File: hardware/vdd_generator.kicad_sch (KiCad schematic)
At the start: 26 parts, among them Q1 BC547, Q2 BC327, Q3 BC327, Q4 BC327, U2 74LS06N

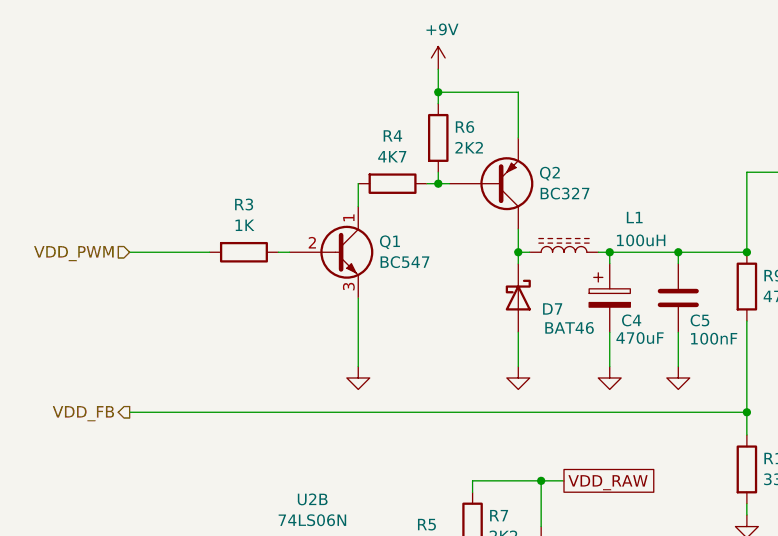
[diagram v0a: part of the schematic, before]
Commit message: Rev.E. Updated hardware design.
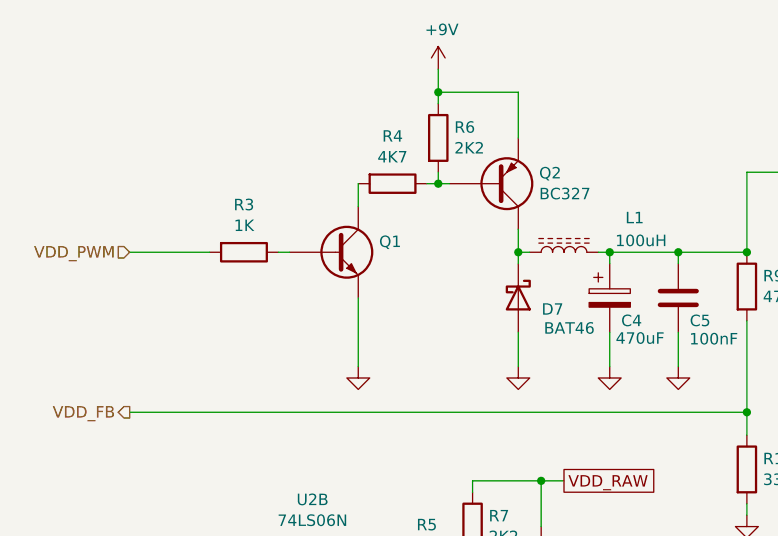
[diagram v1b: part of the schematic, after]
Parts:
- Q1: value BC547 -> (none); footprint Package_TO_SOT_THT:TO-92_Inline_Wide -> (none)
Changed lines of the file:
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@@
   (title_block
     (title "USB Flash/EPROM Programmer")
-    (date "2022-04-23")
+    (date "2022-04-27")
     (rev "v0.1.0 rev.E")
     (company "Robson Martins")
@@
       (effects (font (size 1.27 1.27)) (justify left))
     )
-    (property "Value" "BC547" (id 1) (at 62.0014 48.133 0)
-      (effects (font (size 1.27 1.27)) (justify left))
-    )
-    (property "Footprint" "Package_TO_SOT_THT:TO-92_Inline_Wide" (id 2) (at 62.23 48.895 0)
+    (property "Value" "" (id 1) (at 62.0014 48.133 0)
+      (effects (font (size 1.27 1.27)) (justify left))
+    )
+    (property "Footprint" "" (id 2) (at 62.23 48.895 0)
       (effects (font (size 1.27 1.27) italic) (justify left) hide)
     )

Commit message: Rev.E. Updated specifications document and hardware design.
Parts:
- C4: footprint Capacitor_THT:CP_Radial_D10.0mm_P7.50mm -> (none)
- C6: footprint Capacitor_THT:CP_Radial_D8.0mm_P3.50mm -> (none)
- Q2, Q3, Q4: value BC327 -> (none); footprint Package_TO_SOT_THT:TO-92_Inline_Wide -> (none)
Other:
- note added: "1/2W"
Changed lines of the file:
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@@
     (stroke (width 0) (type default) (color 0 0 0 0))
+  )
+  (text "1/2W" (at 138.43 77.47 0)
+    (effects (font (size 1.27 1.27)) (justify left bottom))
   )
   (text "5V1\n1W" (at 152.4 86.36 0)
@@
       (effects (font (size 1.27 1.27)) (justify left))
     )
-    (property "Footprint" "Capacitor_THT:CP_Radial_D10.0mm_P7.50mm" (id 2) (at 88.5952 55.88 0)
+    (property "Footprint" "" (id 2) (at 88.5952 55.88 0)
       (effects (font (size 1.27 1.27)) hide)
     )
@@
       (effects (font (size 1.27 1.27)) (justify left))
     )
-    (property "Value" "BC327" (id 1) (at 79.7814 40.513 0)
-      (effects (font (size 1.27 1.27)) (justify left))
-    )
-    (property "Footprint" "Package_TO_SOT_THT:TO-92_Inline_Wide" (id 2) (at 80.01 37.465 0)
+    (property "Value" "" (id 1) (at 79.7814 40.513 0)
+      (effects (font (size 1.27 1.27)) (justify left))
+    )
+    (property "Footprint" "" (id 2) (at 80.01 37.465 0)
       (effects (font (size 1.27 1.27) italic) (justify left) hide)
     )
@@
       (effects (font (size 1.27 1.27)) (justify left))
     )
-    (property "Value" "BC327" (id 1) (at 169.9514 48.133 0)
-      (effects (font (size 1.27 1.27)) (justify left))
-    )
-    (property "Footprint" "Package_TO_SOT_THT:TO-92_Inline_Wide" (id 2) (at 170.18 45.085 0)
+    (property "Value" "" (id 1) (at 169.9514 48.133 0)
+      (effects (font (size 1.27 1.27)) (justify left))
+    )
+    (property "Footprint" "" (id 2) (at 170.18 45.085 0)
       (effects (font (size 1.27 1.27) italic) (justify left) hide)
     )
@@
       (effects (font (size 1.27 1.27)) (justify left))
     )
-    (property "Footprint" "Capacitor_THT:CP_Radial_D8.0mm_P3.50mm" (id 2) (at 168.6052 83.82 0)
+    (property "Footprint" "" (id 2) (at 168.6052 83.82 0)
       (effects (font (size 1.27 1.27)) hide)
     )
@@
       (effects (font (size 1.27 1.27)) (justify left))
     )
-    (property "Value" "BC327" (id 1) (at 82.3214 83.693 0)
-      (effects (font (size 1.27 1.27)) (justify left))
-    )
-    (property "Footprint" "Package_TO_SOT_THT:TO-92_Inline_Wide" (id 2) (at 82.55 80.645 0)
+    (property "Value" "" (id 1) (at 82.3214 83.693 0)
+      (effects (font (size 1.27 1.27)) (justify left))
+    )
+    (property "Footprint" "" (id 2) (at 82.55 80.645 0)
       (effects (font (size 1.27 1.27) italic) (justify left) hide)
     )

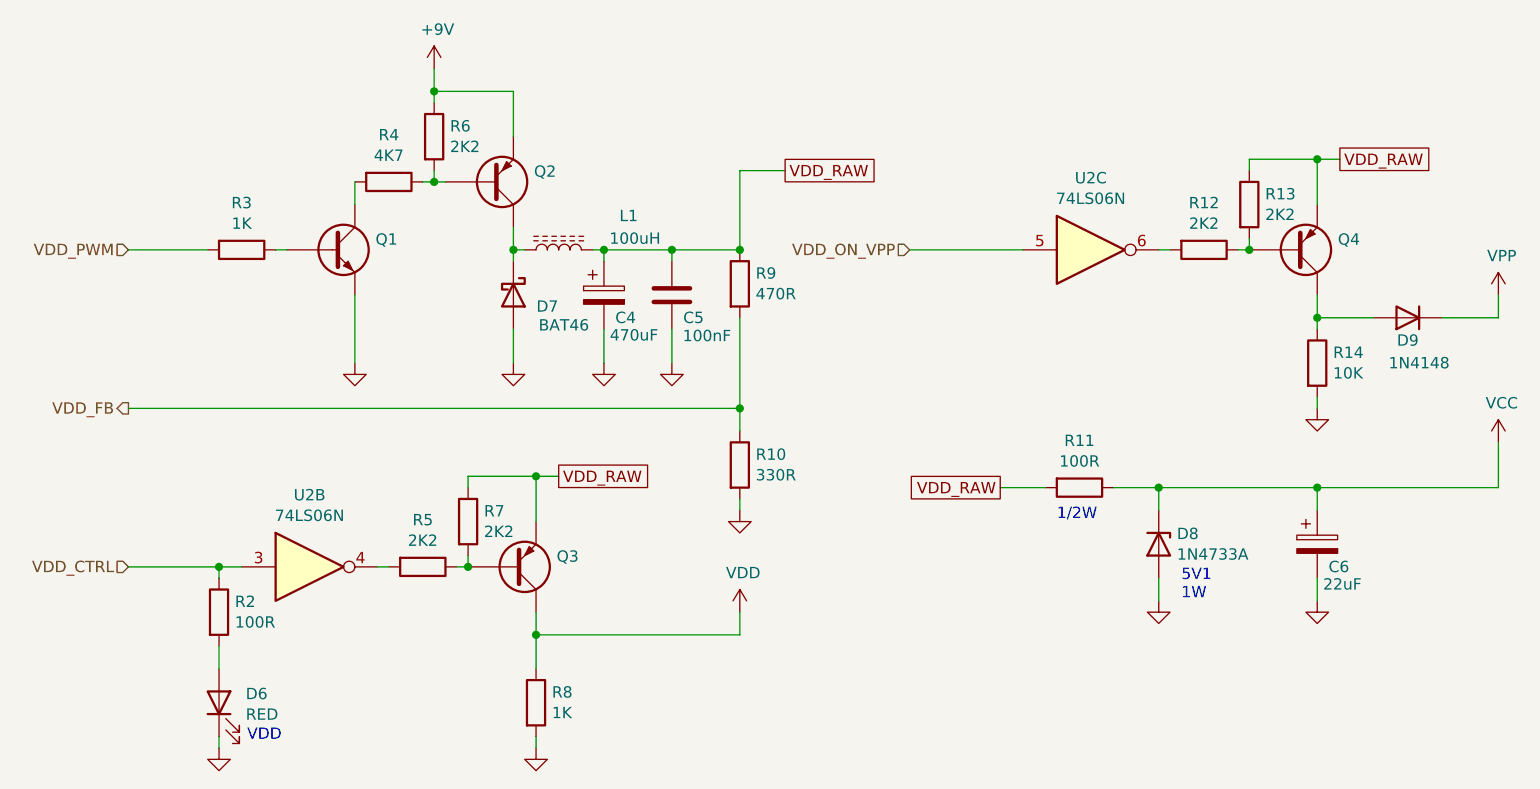
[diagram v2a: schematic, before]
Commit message: Rev.E. Updated R51 wattage.
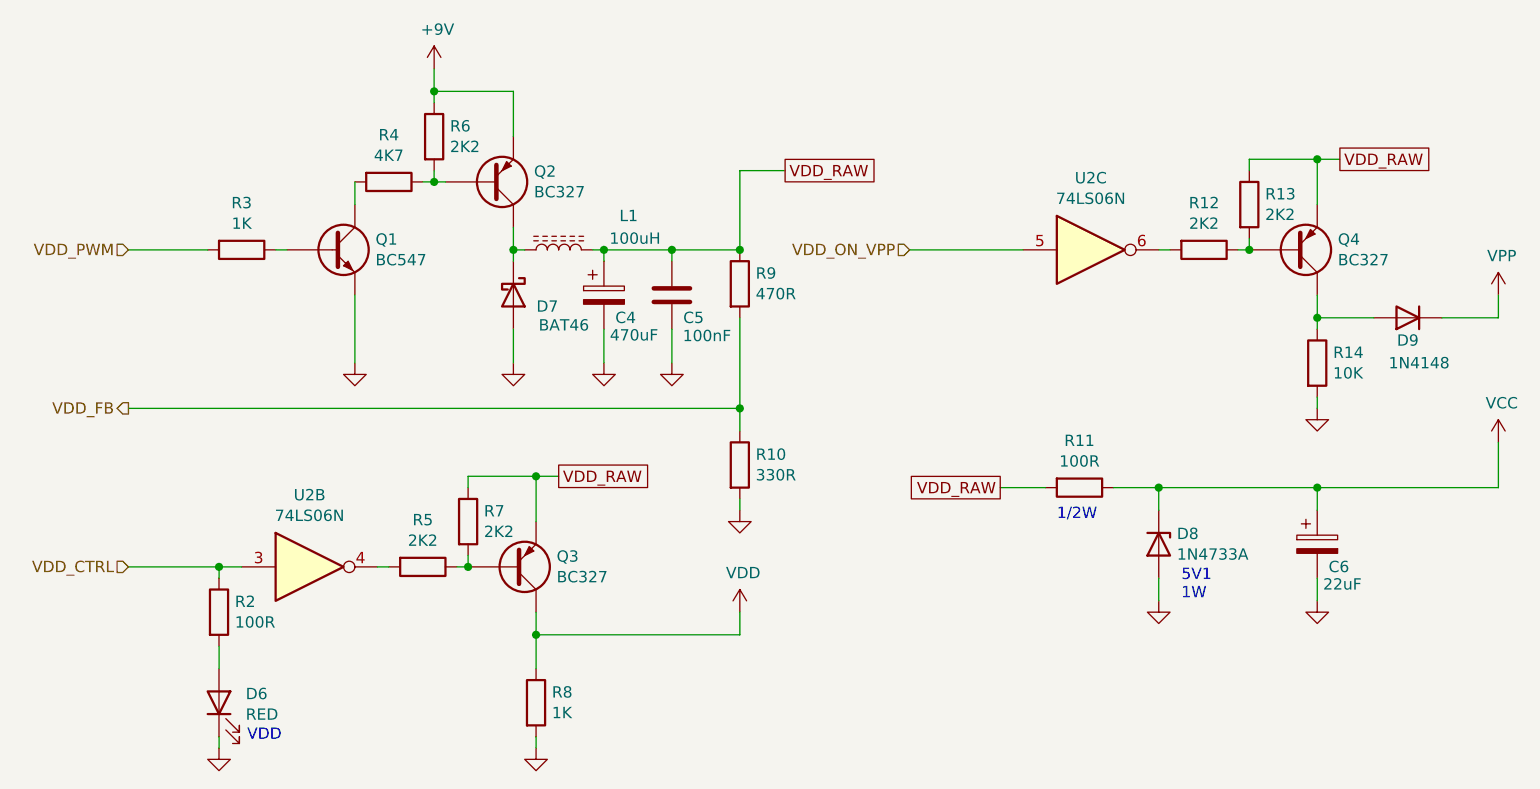
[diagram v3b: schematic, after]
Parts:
- C4: footprint (none) -> Capacitor_THT:CP_Radial_D8.0mm_P3.80mm
- C6: footprint (none) -> Capacitor_THT:CP_Radial_D5.0mm_P2.50mm
- Q1: value (none) -> BC547; footprint (none) -> Package_TO_SOT_THT:TO-92_Inline_Wide
- Q2, Q3, Q4: value (none) -> BC327; footprint (none) -> Package_TO_SOT_THT:TO-92_Inline_Wide
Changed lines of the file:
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@@
       (effects (font (size 1.27 1.27)) (justify left))
     )
-    (property "Footprint" "" (id 2) (at 88.5952 55.88 0)
+    (property "Footprint" "Capacitor_THT:CP_Radial_D8.0mm_P3.80mm" (id 2) (at 88.5952 55.88 0)
       (effects (font (size 1.27 1.27)) hide)
     )
@@
       (effects (font (size 1.27 1.27)) (justify left))
     )
-    (property "Value" "" (id 1) (at 79.7814 40.513 0)
-      (effects (font (size 1.27 1.27)) (justify left))
-    )
-    (property "Footprint" "" (id 2) (at 80.01 37.465 0)
+    (property "Value" "BC327" (id 1) (at 79.7814 40.513 0)
+      (effects (font (size 1.27 1.27)) (justify left))
+    )
+    (property "Footprint" "Package_TO_SOT_THT:TO-92_Inline_Wide" (id 2) (at 80.01 37.465 0)
       (effects (font (size 1.27 1.27) italic) (justify left) hide)
     )
@@
       (effects (font (size 1.27 1.27)) (justify left))
     )
-    (property "Value" "" (id 1) (at 62.0014 48.133 0)
-      (effects (font (size 1.27 1.27)) (justify left))
-    )
-    (property "Footprint" "" (id 2) (at 62.23 48.895 0)
+    (property "Value" "BC547" (id 1) (at 62.0014 48.133 0)
+      (effects (font (size 1.27 1.27)) (justify left))
+    )
+    (property "Footprint" "Package_TO_SOT_THT:TO-92_Inline_Wide" (id 2) (at 62.23 48.895 0)
       (effects (font (size 1.27 1.27) italic) (justify left) hide)
     )
@@
       (effects (font (size 1.27 1.27)) (justify left))
     )
-    (property "Value" "" (id 1) (at 169.9514 48.133 0)
-      (effects (font (size 1.27 1.27)) (justify left))
-    )
-    (property "Footprint" "" (id 2) (at 170.18 45.085 0)
+    (property "Value" "BC327" (id 1) (at 169.9514 48.133 0)
+      (effects (font (size 1.27 1.27)) (justify left))
+    )
+    (property "Footprint" "Package_TO_SOT_THT:TO-92_Inline_Wide" (id 2) (at 170.18 45.085 0)
       (effects (font (size 1.27 1.27) italic) (justify left) hide)
     )
@@
       (effects (font (size 1.27 1.27)) (justify left))
     )
-    (property "Footprint" "" (id 2) (at 168.6052 83.82 0)
+    (property "Footprint" "Capacitor_THT:CP_Radial_D5.0mm_P2.50mm" (id 2) (at 168.6052 83.82 0)
       (effects (font (size 1.27 1.27)) hide)
     )
@@
       (effects (font (size 1.27 1.27)) (justify left))
     )
-    (property "Value" "" (id 1) (at 82.3214 83.693 0)
-      (effects (font (size 1.27 1.27)) (justify left))
-    )
-    (property "Footprint" "" (id 2) (at 82.55 80.645 0)
+    (property "Value" "BC327" (id 1) (at 82.3214 83.693 0)
+      (effects (font (size 1.27 1.27)) (justify left))
+    )
+    (property "Footprint" "Package_TO_SOT_THT:TO-92_Inline_Wide" (id 2) (at 82.55 80.645 0)
       (effects (font (size 1.27 1.27) italic) (justify left) hide)
     )

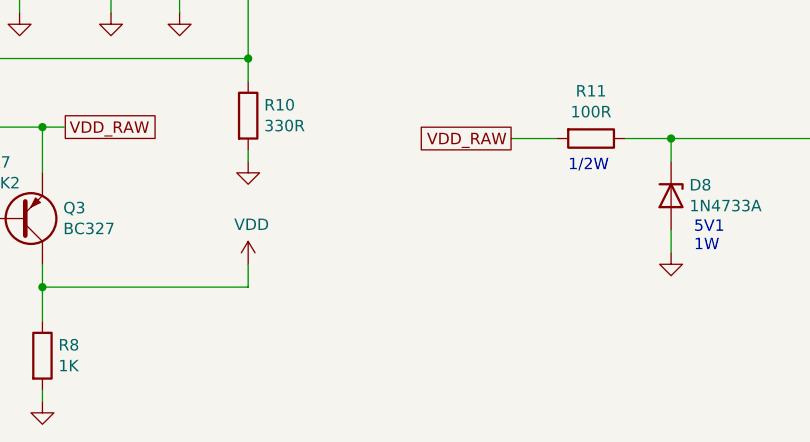
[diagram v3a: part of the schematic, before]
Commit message: Rev.E. Add Test Points for VDD/VPP/GND.
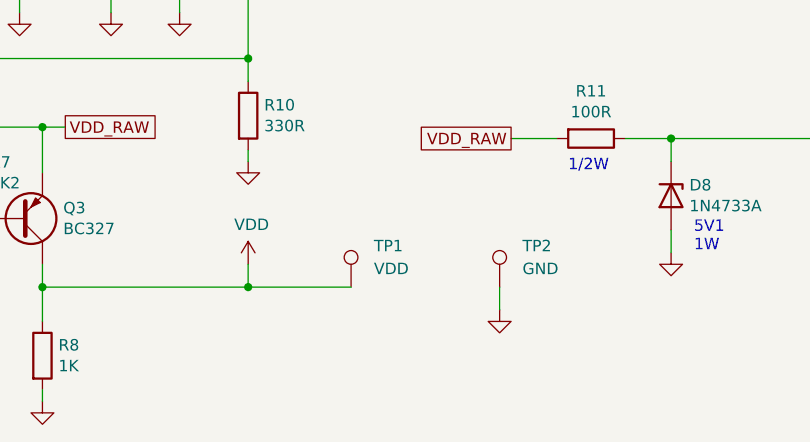
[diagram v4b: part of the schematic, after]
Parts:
- added TP1: VDD, TestPoint:TestPoint_THTPad_2.5x2.5mm_Drill1.2mm, symbol Connector:TestPoint
- added TP2: GND, TestPoint:TestPoint_THTPad_2.5x2.5mm_Drill1.2mm, symbol Connector:TestPoint
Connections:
- net GND: now also TP2.1
- net VDD: now also TP1.1
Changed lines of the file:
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@@
   (junction (at 149.86 73.66) (diameter 0) (color 0 0 0 0)
   )
+  (junction (at 102.87 90.17) (diameter 0) (color 0 0 0 0)
+  )
   (junction (at 160.02 46.99) (diameter 0) (color 0 0 0 0)
   )
@@
     (stroke (width 0) (type default) (color 0 0 0 0))
   )
+  (wire (pts (xy 102.87 90.17) (xy 114.3 90.17))
+    (stroke (width 0) (type default) (color 0 0 0 0))
+  )
   (wire (pts (xy 44.45 82.55) (xy 34.29 82.55))
     (stroke (width 0) (type default) (color 0 0 0 0))
@@
   )
   (wire (pts (xy 72.39 81.28) (xy 72.39 82.55))
+    (stroke (width 0) (type default) (color 0 0 0 0))
+  )
+  (wire (pts (xy 130.81 90.17) (xy 130.81 92.71))
     (stroke (width 0) (type default) (color 0 0 0 0))
   )
@@
       (effects (font (size 1.27 1.27)) hide)
     )
-    (pin "1")
-    (pin "2")
     (pin "3")
     (pin "4")
-    (pin "5")
-    (pin "6")
-    (pin "8")
-    (pin "9")
-    (pin "10")
-    (pin "11")
-    (pin "12")
-    (pin "13")
-    (pin "14")
-    (pin "7")
   )
   (symbol (lib_id "Device:R") (at 67.31 82.55 270) (unit 1)
@@
       (effects (font (size 1.27 1.27)) hide)
     )
-    (pin "1")
-    (pin "2")
-    (pin "3")
-    (pin "4")
     (pin "5")
     (pin "6")
-    (pin "8")
-    (pin "9")
-    (pin "10")
-    (pin "11")
-    (pin "12")
-    (pin "13")
-    (pin "14")
-    (pin "7")
   )
   (symbol (lib_id "Device:R") (at 154.94 46.99 270) (unit 1)
@@
     (pin "3")
   )
+  (symbol (lib_id "Connector:TestPoint") (at 114.3 90.17 0) (unit 1)
+    (in_bom yes) (on_board yes) (fields_autoplaced)
+    (property "Reference" "TP1" (id 0) (at 116.84 85.5979 0)
+      (effects (font (size 1.27 1.27)) (justify left))
+    )
+    (property "Value" "VDD" (id 1) (at 116.84 88.1379 0)
+      (effects (font (size 1.27 1.27)) (justify left))
+    )
+    (property "Footprint" "TestPoint:TestPoint_THTPad_2.5x2.5mm_Drill1.2mm" (id 2) (at 119.38 90.17 0)
+      (effects (font (size 1.27 1.27)) hide)
+    )
+    (property "Datasheet" "~" (id 3) (at 119.38 90.17 0)
+      (effects (font (size 1.27 1.27)) hide)
+    )
+    (pin "1")
+  )
+  (symbol (lib_id "Connector:TestPoint") (at 130.81 90.17 0) (unit 1)
+    (in_bom yes) (on_board yes) (fields_autoplaced)
+    (property "Reference" "TP2" (id 0) (at 133.35 85.5979 0)
+      (effects (font (size 1.27 1.27)) (justify left))
+    )
+    (property "Value" "GND" (id 1) (at 133.35 88.1379 0)
+      (effects (font (size 1.27 1.27)) (justify left))
+    )
+    (property "Footprint" "TestPoint:TestPoint_THTPad_2.5x2.5mm_Drill1.2mm" (id 2) (at 135.89 90.17 0)
+      (effects (font (size 1.27 1.27)) hide)
+    )
+    (property "Datasheet" "~" (id 3) (at 135.89 90.17 0)
+      (effects (font (size 1.27 1.27)) hide)
+    )
+    (pin "1")
+  )
+  (symbol (lib_id "power:GND") (at 130.81 92.71 0) (unit 1)
+    (in_bom yes) (on_board yes)
+    (property "Reference" "#PWR080" (id 0) (at 130.81 99.06 0)
+      (effects (font (size 1.27 1.27)) hide)
+    )
+    (property "Value" "GND" (id 1) (at 130.937 97.1042 0)
+      (effects (font (size 1.27 1.27)) hide)
+    )
+    (property "Footprint" "" (id 2) (at 130.81 92.71 0)
+      (effects (font (size 1.27 1.27)) hide)
+    )
+    (property "Datasheet" "" (id 3) (at 130.81 92.71 0)
+      (effects (font (size 1.27 1.27)) hide)
+    )
+    (pin "1")
+  )
 )
